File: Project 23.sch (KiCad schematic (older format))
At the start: 59 parts, among them J11 SRX 1, J12 SRX 2, J13 SWD, J14 Serial DB, J21 BATT +, J22 BATT-, J61 USB_Micro, J71 Micro_SD_Card_Det, SW11 UI_Btn, SW12 PWR_BTN, U1 STM32F103C8T7, U21 MCP73832, U3 NCP551, U32 MIC5504, U4 NCP1402, U5 oled, Y11 8 MHz

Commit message: Finished footprint for micro SD holder
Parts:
- removed J14: Serial DB, symbol Connector:Conn_01x03_Female
- added TP31: 3V3SB, TestPoint:TestPoint_Pad_D2.0mm, symbol Connector:TestPoint
- added TP32: 3V3, TestPoint:TestPoint_Pad_D2.0mm, symbol Connector:TestPoint
- added TP41: 5V, TestPoint:TestPoint_Pad_D2.0mm, symbol Connector:TestPoint
- added TP73: TXD, TestPoint:TestPoint_Pad_D2.0mm, symbol Connector:TestPoint
- added TP74: RXD, TestPoint:TestPoint_Pad_D2.0mm, symbol Connector:TestPoint
- added TP75: GND, TestPoint:TestPoint_Pad_D2.0mm, symbol Connector:TestPoint
- J11, J12: symbol Project-23-rescue:Conn_02x05_Odd_Even -> Project-23-rescue:Conn_02x05_Odd_Even-Project-23-rescue
- J13: symbol Project-23-rescue:Conn_01x04 -> Project-23-rescue:Conn_01x04-Project-23-rescue
- J21, J22: footprint (none) -> Connector_PinHeader_2.54mm:PinHeader_1x01_P2.54mm_Vertical
- J61: symbol Project-23-rescue:USB_OTG -> Project-23-rescue:USB_OTG-Project-23-rescue
- J71: footprint (none) -> Project 23:micro sd holder
- R15, R16, R21, R22, R81, R82, R83, R84: footprint (none) -> Resistor_SMD:R_0805_2012Metric_Pad1.15x1.40mm_HandSolder
- SW11, SW12: symbol Project-23-rescue:SW_SPST -> Project-23-rescue:SW_SPST-Project-23-rescue
- U21: footprint (none) -> Package_TO_SOT_SMD:SOT-23-5_HandSoldering
- U5: symbol Project-23-rescue:Conn_01x07 -> Project-23-rescue:Conn_01x07-Project-23-rescue
- renumbered U3 to U31, U4 to U41
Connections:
- wire segments 320 -> 324
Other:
- moved on the sheet: C31, C32, C33, C34, U31, U32

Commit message: Completed V0.7 PCB Design
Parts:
- removed R64: 10k, Resistor_SMD:R_0805_2012Metric_Pad1.15x1.40mm_HandSolder, symbol Device:R
- removed TP73: TXD, TestPoint:TestPoint_Pad_D2.0mm, symbol Connector:TestPoint
- removed TP74: RXD, TestPoint:TestPoint_Pad_D2.0mm, symbol Connector:TestPoint
- added H1, H2, H3, H4: M2, MountingHole:MountingHole_2.2mm_M2, symbol Mechanical:MountingHole
- J61: footprint Project 23:usbMicro -> Project 23:microUsbSunken
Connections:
- net labels added: Stat
- net labels removed: BATT_Mon, VBus_Sense
- wire segments 324 -> 321
- no-connect marks 15 -> 14
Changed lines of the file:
@@
 Pwr_LED
 Text Label 8350 1700 0    60   ~ 0
-PWR_EN
+PWR_En
 $Comp
 L Device:C C16
@@
 F 0 "J61" H 15300 9200 50  0000 L CNN
 F 1 "USB_Micro" H 15300 9100 50  0000 L CNN
-F 2 "Project 23:usbMicro" H 15650 8700 50  0001 C CNN
+F 2 "Project 23:microUsbSunken" H 15650 8700 50  0001 C CNN
 F 3 "" H 15650 8700 50  0001 C CNN
 	1    15500 8750
@@
 	0    1    1    0
 $EndComp
-$Comp
-L Device:R R64
-U 1 1 5B06806B
-P 14700 8550
-F 0 "R64" V 14600 8550 50  0000 C CNN
-F 1 "10k" V 14700 8550 50  0000 C CNN
-F 2 "Resistor_SMD:R_0805_2012Metric_Pad1.15x1.40mm_HandSolder" V 14630 8550 50  0001 C CNN
-F 3 "" H 14700 8550 50  0001 C CNN
-	1    14700 8550
-	0    1    1    0
-$EndComp
-Text Label 14050 8550 0    60   ~ 0
-VBus_Sense
 NoConn ~ 950  1500
 $Comp
@@
 	15150 9200 15500 9200
 Wire Wire Line
-	14850 8550 15100 8550
-Wire Wire Line
 	14450 8750 14450 8950
 Connection ~ 14450 8750
 Connection ~ 15150 9200
-Connection ~ 15100 8550
-Wire Wire Line
-	14550 8550 14050 8550
 Wire Wire Line
 	13400 3300 13350 3300
@@
 	1    0    0    -1
 $EndComp
-NoConn ~ 1450 2700
 NoConn ~ 1450 2800
 Text Label 3300 9500 0    60   ~ 0
@@
 Batt_Mon
 Text Label 4150 7400 0    60   ~ 0
-BATT_Mon
+Batt_Mon
 Wire Wire Line
 	6200 7350 6200 7400
@@
 $EndComp
 Wire Wire Line
-	7700 7150 7250 7150
-Wire Wire Line
-	7700 7350 7250 7350
-Wire Wire Line
 	7700 7550 7600 7550
 Wire Wire Line
 	7600 7550 7600 7650
-Text Label 7250 7150 0    60   ~ 0
-TXD
-Text Label 7250 7350 0    60   ~ 0
-RXD
 $Comp
 L power:GND #PWR0115
@@
 	1    7600 7650
 	1    0    0    -1
-$EndComp
-$Comp
-L Connector:TestPoint TP73
-U 1 1 5C096841
-P 7700 7150
-F 0 "TP73" V 7654 7338 50  0000 L CNN
-F 1 "TXD" V 7745 7338 50  0000 L CNN
-F 2 "TestPoint:TestPoint_Pad_D2.0mm" H 7900 7150 50  0001 C CNN
-F 3 "~" H 7900 7150 50  0001 C CNN
-	1    7700 7150
-	0    1    1    0
-$EndComp
-$Comp
-L Connector:TestPoint TP74
-U 1 1 5C0CDC40
-P 7700 7350
-F 0 "TP74" V 7654 7538 50  0000 L CNN
-F 1 "RXD" V 7745 7538 50  0000 L CNN
-F 2 "TestPoint:TestPoint_Pad_D2.0mm" H 7900 7350 50  0001 C CNN
-F 3 "~" H 7900 7350 50  0001 C CNN
-	1    7700 7350
-	0    1    1    0
 $EndComp
 $Comp
@@
 Wire Wire Line
 	15350 2700 15550 2700
+$Comp
+L Mechanical:MountingHole H1
+U 1 1 5C0E81B8
+P 9400 7700
+F 0 "H1" H 9500 7746 50  0000 L CNN
+F 1 "M2" H 9500 7655 50  0000 L CNN
+F 2 "MountingHole:MountingHole_2.2mm_M2" H 9400 7700 50  0001 C CNN
+F 3 "~" H 9400 7700 50  0001 C CNN
+	1    9400 7700
+	1    0    0    -1
+$EndComp
+$Comp
+L Mechanical:MountingHole H2
+U 1 1 5C0E8A06
+P 9400 7950
+F 0 "H2" H 9500 7996 50  0000 L CNN
+F 1 "M2" H 9500 7905 50  0000 L CNN
+F 2 "MountingHole:MountingHole_2.2mm_M2" H 9400 7950 50  0001 C CNN
+F 3 "~" H 9400 7950 50  0001 C CNN
+	1    9400 7950
+	1    0    0    -1
+$EndComp
+$Comp
+L Mechanical:MountingHole H3
+U 1 1 5C0E8C1D
+P 9800 7700
+F 0 "H3" H 9900 7746 50  0000 L CNN
+F 1 "M2" H 9900 7655 50  0000 L CNN
+F 2 "MountingHole:MountingHole_2.2mm_M2" H 9800 7700 50  0001 C CNN
+F 3 "~" H 9800 7700 50  0001 C CNN
+	1    9800 7700
+	1    0    0    -1
+$EndComp
+$Comp
+L Mechanical:MountingHole H4
+U 1 1 5C0E8C24
+P 9800 7950
+F 0 "H4" H 9900 7996 50  0000 L CNN
+F 1 "M2" H 9900 7905 50  0000 L CNN
+F 2 "MountingHole:MountingHole_2.2mm_M2" H 9800 7950 50  0001 C CNN
+F 3 "~" H 9800 7950 50  0001 C CNN
+	1    9800 7950
+	1    0    0    -1
+$EndComp
+Text Label 13300 4900 0    60   ~ 0
+Stat
+Wire Wire Line
+	1450 2700 950  2700
+Text Label 950  2700 0    60   ~ 0
+Stat
 $EndSCHEMATC

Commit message: Final prototype v0.7
Added logo, replaced NCP1402 as it is EOL.
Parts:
- removed C41: 10uF,Tan, Capacitor_Tantalum_SMD:CP_EIA-3528-21_Kemet-B_Pad1.50x2.35mm_HandSolder, symbol Device:CP
- removed C42: 47uF,Tan, Capacitor_Tantalum_SMD:CP_EIA-6032-28_Kemet-C_Pad2.25x2.35mm_HandSolder, symbol Device:CP
- removed D41: MBRS140, Diode_SMD:D_SMA_Handsoldering, symbol Device:D_Schottky
- removed U41: NCP1402, Package_TO_SOT_SMD:SOT-23-5_HandSoldering, symbol Project23-extras:NCP1402
- added C41, C42: 10uF, Capacitor_SMD:C_0805_2012Metric_Pad1.15x1.40mm_HandSolder, symbol Device:C
- added U2: 74AHCT1G125, Package_TO_SOT_SMD:SOT-23-5_HandSoldering, symbol 74xGxx:74AHC1G125
- added U41: TPS6122x, Package_TO_SOT_SMD:SOT-363_SC-70-6_Handsoldering, symbol Project23-extras:TPS6122x
- L41: value 47uH -> 4.7uH; footprint Inductor_SMD:L_1210_3225Metric_Pad1.42x2.65mm_HandSolder -> Inductor_SMD:L_1206_3216Metric_Pad1.42x1.75mm_HandSolder
- R21: value 10k -> 5K1
- U5: footprint Connector_PinSocket_2.54mm:PinSocket_1x07_P2.54mm_Vertical -> Connector_PinHeader_2.54mm:PinHeader_1x07_P2.54mm_Vertical
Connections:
- net labels added: VCC
- net labels removed: PWR_En, RXD, TXD, VDD
- wire segments 321 -> 335
- no-connect marks 14 -> 15

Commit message: Power Routed
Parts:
- J11, J12: symbol Project-23-rescue:Conn_02x05_Odd_Even-Project-23-rescue -> Project-23-rescue:Conn_02x05_Odd_Even-Project-23-rescue-Project-23-rescue
- J13: symbol Project-23-rescue:Conn_01x04-Project-23-rescue -> Project-23-rescue:Conn_01x04-Project-23-rescue-Project-23-rescue
- J61: symbol Project-23-rescue:USB_OTG-Project-23-rescue -> Project-23-rescue:USB_OTG-Project-23-rescue-Project-23-rescue
- SW11, SW12: symbol Project-23-rescue:SW_SPST-Project-23-rescue -> Project-23-rescue:SW_SPST-Project-23-rescue-Project-23-rescue
- U5: symbol Project-23-rescue:Conn_01x07-Project-23-rescue -> Project-23-rescue:Conn_01x07-Project-23-rescue-Project-23-rescue
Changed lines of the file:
@@
 Rev_Limit
 $Comp
-L Project-23-rescue:Conn_02x05_Odd_Even-Project-23-rescue J11
+L Project-23-rescue:Conn_02x05_Odd_Even-Project-23-rescue-Project-23-rescue J11
 U 1 1 5B049189
 P 2350 9400
@@
 $EndComp
 $Comp
-L Project-23-rescue:Conn_02x05_Odd_Even-Project-23-rescue J12
+L Project-23-rescue:Conn_02x05_Odd_Even-Project-23-rescue-Project-23-rescue J12
 U 1 1 5B049278
 P 2350 10350
@@
 Fwd_Limit
 $Comp
-L Project-23-rescue:SW_SPST-Project-23-rescue SW11
+L Project-23-rescue:SW_SPST-Project-23-rescue-Project-23-rescue SW11
 U 1 1 5B04BEBC
 P 6700 9950
@@
 UI_Btn
 $Comp
-L Project-23-rescue:SW_SPST-Project-23-rescue SW12
+L Project-23-rescue:SW_SPST-Project-23-rescue-Project-23-rescue SW12
 U 1 1 5B04C643
 P 6700 10250
@@
 Power_Btn
 $Comp
-L Project-23-rescue:Conn_01x04-Project-23-rescue J13
+L Project-23-rescue:Conn_01x04-Project-23-rescue-Project-23-rescue J13
 U 1 1 5B04CC06
 P 5050 10200
@@
 $EndComp
 $Comp
-L Project-23-rescue:Conn_01x07-Project-23-rescue U5
+L Project-23-rescue:Conn_01x07-Project-23-rescue-Project-23-rescue U5
 U 1 1 5B057DA1
 P 10050 9950
@@
 Pwr_LED
 $Comp
-L Project-23-rescue:USB_OTG-Project-23-rescue J61
+L Project-23-rescue:USB_OTG-Project-23-rescue-Project-23-rescue J61
 U 1 1 5B05AAC7
 P 15500 8750

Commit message: Power lines routed
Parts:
- J11, J12: symbol Project-23-rescue:Conn_02x05_Odd_Even-Project-23-rescue-Project-23-rescue -> Project-23-rescue:Conn_02x05_Odd_Even-Project-23-rescue
- J13: symbol Project-23-rescue:Conn_01x04-Project-23-rescue-Project-23-rescue -> Project-23-rescue:Conn_01x04-Project-23-rescue
- J61: symbol Project-23-rescue:USB_OTG-Project-23-rescue-Project-23-rescue -> Project-23-rescue:USB_OTG-Project-23-rescue
- SW11, SW12: symbol Project-23-rescue:SW_SPST-Project-23-rescue-Project-23-rescue -> Project-23-rescue:SW_SPST-Project-23-rescue
- U5: symbol Project-23-rescue:Conn_01x07-Project-23-rescue-Project-23-rescue -> Project-23-rescue:Conn_01x07-Project-23-rescue
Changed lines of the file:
@@
 Rev_Limit
 $Comp
-L Project-23-rescue:Conn_02x05_Odd_Even-Project-23-rescue-Project-23-rescue J11
+L Project-23-rescue:Conn_02x05_Odd_Even-Project-23-rescue J11
 U 1 1 5B049189
 P 2350 9400
@@
 $EndComp
 $Comp
-L Project-23-rescue:Conn_02x05_Odd_Even-Project-23-rescue-Project-23-rescue J12
+L Project-23-rescue:Conn_02x05_Odd_Even-Project-23-rescue J12
 U 1 1 5B049278
 P 2350 10350
@@
 Fwd_Limit
 $Comp
-L Project-23-rescue:SW_SPST-Project-23-rescue-Project-23-rescue SW11
+L Project-23-rescue:SW_SPST-Project-23-rescue SW11
 U 1 1 5B04BEBC
 P 6700 9950
@@
 UI_Btn
 $Comp
-L Project-23-rescue:SW_SPST-Project-23-rescue-Project-23-rescue SW12
+L Project-23-rescue:SW_SPST-Project-23-rescue SW12
 U 1 1 5B04C643
 P 6700 10250
@@
 Power_Btn
 $Comp
-L Project-23-rescue:Conn_01x04-Project-23-rescue-Project-23-rescue J13
+L Project-23-rescue:Conn_01x04-Project-23-rescue J13
 U 1 1 5B04CC06
 P 5050 10200
@@
 $EndComp
 $Comp
-L Project-23-rescue:Conn_01x07-Project-23-rescue-Project-23-rescue U5
+L Project-23-rescue:Conn_01x07-Project-23-rescue U5
 U 1 1 5B057DA1
 P 10050 9950
@@
 Pwr_LED
 $Comp
-L Project-23-rescue:USB_OTG-Project-23-rescue-Project-23-rescue J61
+L Project-23-rescue:USB_OTG-Project-23-rescue J61
 U 1 1 5B05AAC7
 P 15500 8750

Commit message: 4 Layer with reworked layout
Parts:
- removed C71: 1uF, Capacitor_SMD:C_0805_2012Metric_Pad1.15x1.40mm_HandSolder, symbol Device:C
- removed D3, D4: LED, LED_SMD:LED_0805_2012Metric_Pad1.15x1.40mm_HandSolder, symbol Device:LED
- removed J11: SRX 1, Connector_PinHeader_1.27mm:PinHeader_2x05_P1.27mm_Horizontal, symbol Project-23-rescue:Conn_02x05_Odd_Even-Project-23-rescue
- removed J71: Micro_SD_Card_Det, Project 23:micro sd holder, symbol Connector:Micro_SD_Card_Det
- removed R83, R84: 10k, Resistor_SMD:R_0805_2012Metric_Pad1.15x1.40mm_HandSolder, symbol Device:R
- removed RN1: 1k, Resistor_SMD:R_Array_Convex_4x0603, symbol Device:R_Pack04
- added C15, C16, C17, C18: 1u, Capacitor_SMD:C_0805_2012Metric_Pad1.15x1.40mm_HandSolder, symbol Device:C
- added J2: SPARK Encoder Port, Connector_JST:JST_PH_S6B-PH-K_1x06_P2.00mm_Horizontal, symbol Connector:Conn_01x06_Male
- added JP1: BOOT1, Jumper:SolderJumper-2_P1.3mm_Open_Pad1.0x1.5mm, symbol Device:Jumper_NO_Small
- added JP2: Reset, Jumper:SolderJumper-2_P1.3mm_Open_Pad1.0x1.5mm, symbol Device:Jumper_NO_Small
- added JP3: BOOT0, Jumper:SolderJumper-2_P1.3mm_Open_Pad1.0x1.5mm, symbol Device:Jumper_NO_Small
- added R14: 1.5k, Resistor_SMD:R_0805_2012Metric_Pad1.15x1.40mm_HandSolder, symbol Device:R
- added R15, R16: 10k, Resistor_SMD:R_0805_2012Metric_Pad1.15x1.40mm_HandSolder, symbol Device:R
- C10: renamed from C18; value 0.1uF -> 10n
- C11: renamed from C19; value 0.1uF -> 10n
- C8: renamed from C16; value 0.1uF -> 10n
- C9: renamed from C17; value 0.1uF -> 10n
- D5: renamed from D1; value MBRS140 -> CU10S30; footprint Diode_SMD:D_SMB_Handsoldering -> Diode_SMD:D_SOD-323_HandSoldering
- D6: renamed from D2; value MBRS140 -> CU10S30; footprint Diode_SMD:D_SMB_Handsoldering -> Diode_SMD:D_SOD-323_HandSoldering
- F1: renamed from F12; value 50mA -> 100mA
- F2: renamed from F11; value 50mA -> 100mA
- J1: renamed from J12; symbol Project-23-rescue:Conn_02x05_Odd_Even-Project-23-rescue -> Project-23-rescue:Conn_02x05_Odd_Even-Project-23-rescue-Project-23-rescue
- J3: renamed from J13; symbol Project-23-rescue:Conn_01x04-Project-23-rescue -> Project-23-rescue:Conn_01x04-Project-23-rescue-Project-23-rescue
- J4: renamed from J61; symbol Project-23-rescue:USB_OTG-Project-23-rescue -> Project-23-rescue:USB_OTG-Project-23-rescue-Project-23-rescue
- SW1: renamed from SW11; symbol Project-23-rescue:SW_SPST-Project-23-rescue -> Project-23-rescue:SW_SPST-Project-23-rescue-Project-23-rescue
- SW2: renamed from SW12; symbol Project-23-rescue:SW_SPST-Project-23-rescue -> Project-23-rescue:SW_SPST-Project-23-rescue-Project-23-rescue
- U2: value 74AHCT1G125 -> 74AHC1G125
- U3: renamed from U5; symbol Project-23-rescue:Conn_01x07-Project-23-rescue -> Project-23-rescue:Conn_01x07-Project-23-rescue-Project-23-rescue
- Y1: renamed from Y11; footprint Crystal:Crystal_HC49-4H_Vertical -> Crystal:Crystal_SMD_Abracon_ABM3-2Pin_5.0x3.2mm_HandSoldering
- renumbered C11 to C1, C42 to C12, C22 to C13, C34 to C14, C12 to C2, C31 to C3, C32 to C4, C41 to C5, C21 to C6, C33 to C7, D11 to D1, D5 to D4, J21 to J5, J22 to J6, L41 to L1, R15 to R1, R63 to R10, R61 to R11, R62 to R12, R21 to R13, R16 to R2, R81 to R3, R82 to R4, R12 to R7, R41 to R8, R22 to R9, RN11 to RN1, RN12 to RN2, TP75 to TP1, TP31 to TP2, TP41 to TP3, TP32 to TP4, U31 to U4, U41 to U5, U21 to U6, U32 to U7
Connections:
- net labels added: PWR_EN_3V
- net labels removed: Fwd_LED, MISO2, MOSI2, Rev_LED, SCK2, SD_CD, SS2
- wire segments 335 -> 338
- no-connect marks 15 -> 7
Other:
- moved on the sheet: C10, C11, C8, C9, D1, F1, F2, J1, R1, R2, R8, RN2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

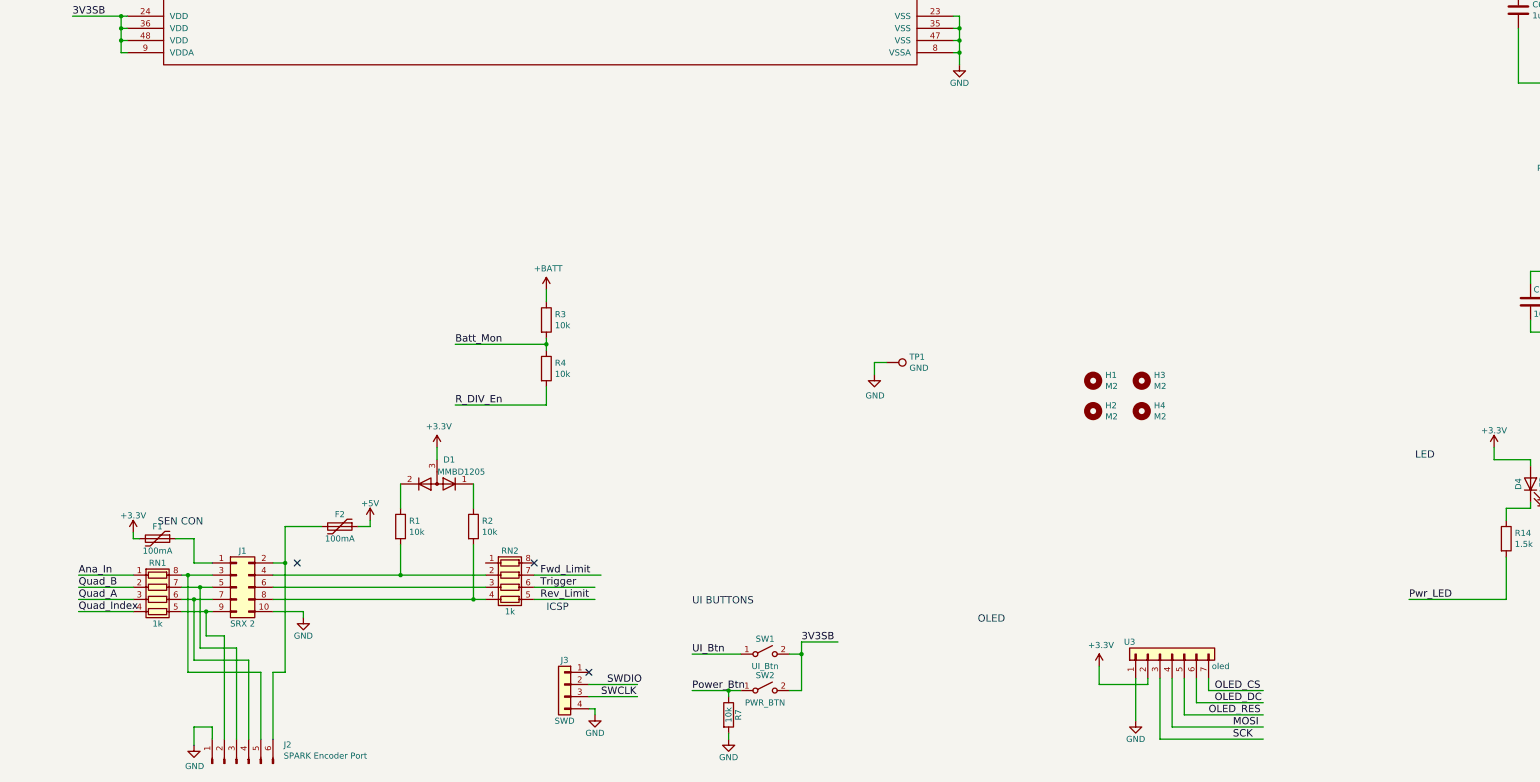
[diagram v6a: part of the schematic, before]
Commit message: Added logo and rearraged silkscreen
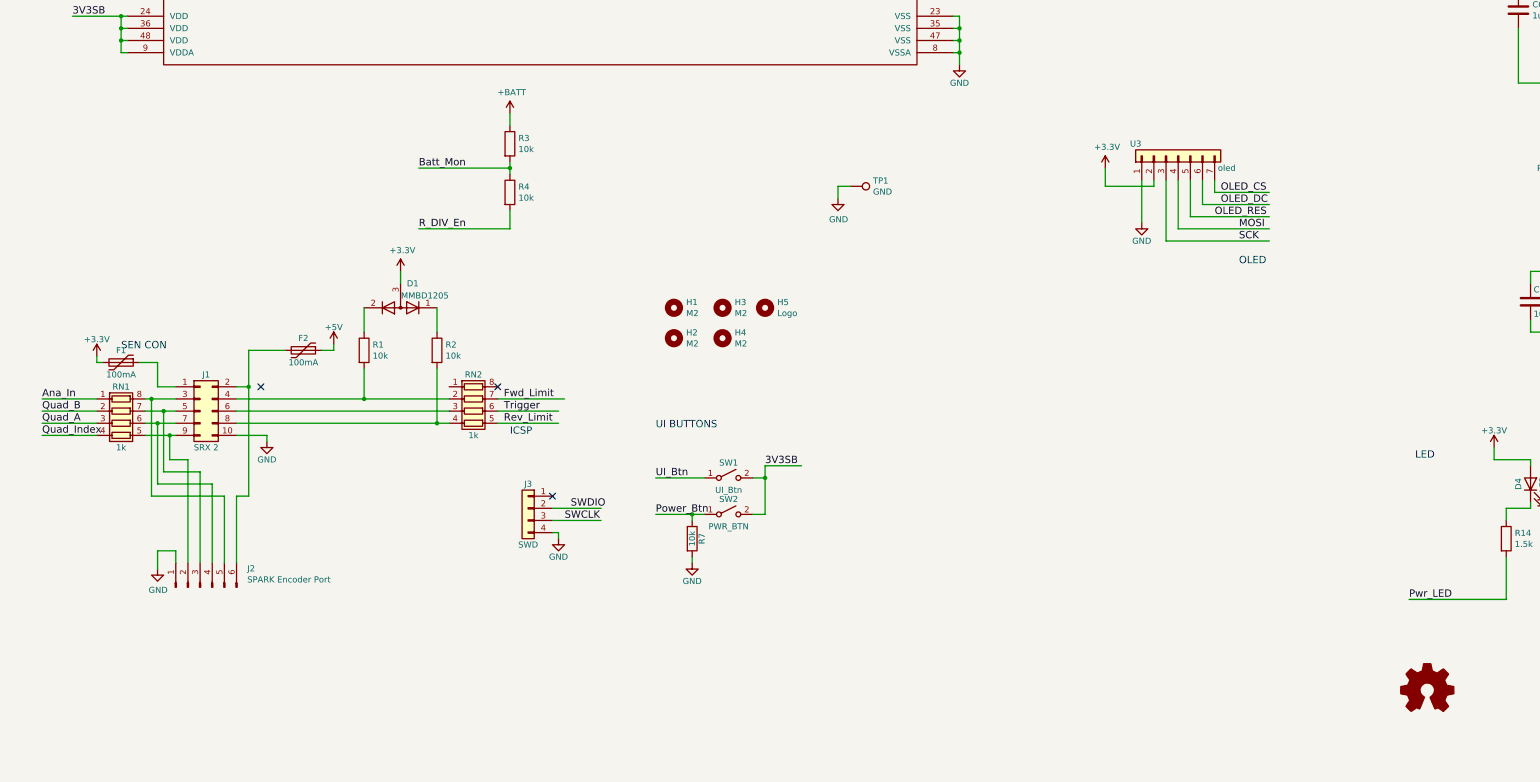
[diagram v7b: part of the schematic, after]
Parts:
- added H5: Logo, Project 23:goldfish, symbol Mechanical:MountingHole
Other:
- moved on the sheet: D1, F1, F2, H1, H2, H3, H4, J1, J2, J3, R1, R2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
